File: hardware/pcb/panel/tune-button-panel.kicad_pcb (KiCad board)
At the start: 2 copper layers, 146 x 71.7 mm, 218 parts, among them J1 USB-C, J1 XIAO left, J2 LiPo, J2 XIAO right, J3 Buttons, J3 LiPo, J4 to XIAO BAT, Q1 AO3401A, SW1 MX switch, SW2 MX switch, SW3 MX switch, SW4 MX switch, SW5 RESET, SW6 BOOT, U1 ESP32-C3-WROOM-02-N4, U2 SRV05-4, U3 TP4054, U4 RT9080-3.3, U5 SRV05-4

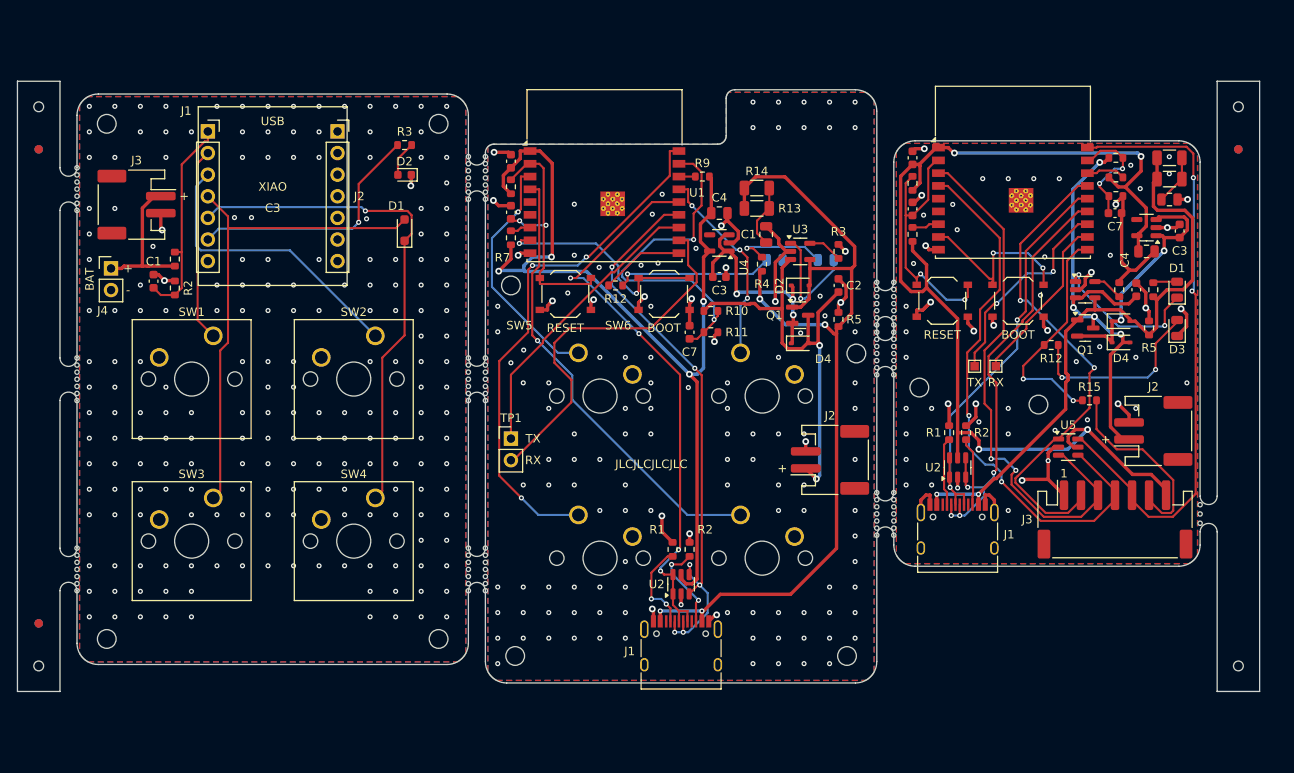
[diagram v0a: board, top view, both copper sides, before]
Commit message: pcb: panel round-1 audit fixes
A 5 mm frame (bars across the top and bottom joining the rails, clear of the overhangs),
so the right rail no longer hangs on one narrow tab. Tabs keep away from mounting holes
(a tab sat on the c3's H4) and leave room for their fillets; bites sit 0.25 mm inside the
board; tab keepouts run 1 mm past the end bites. Fiducials 3.85 mm in (JLC's minimum),
tooling holes with a 1.448 mm mask opening, only the c3's JLC marker kept, panel/fab
cleared before export. free_spans uses fab bodies (the courtyard test was never built).

route.py's crowded_pins now checks every through-hole part not reflowed in paste, not
only those without an LCSC number, so the XIAO sockets stay covered now that JLC fits
them. All three boards replay clean under it.
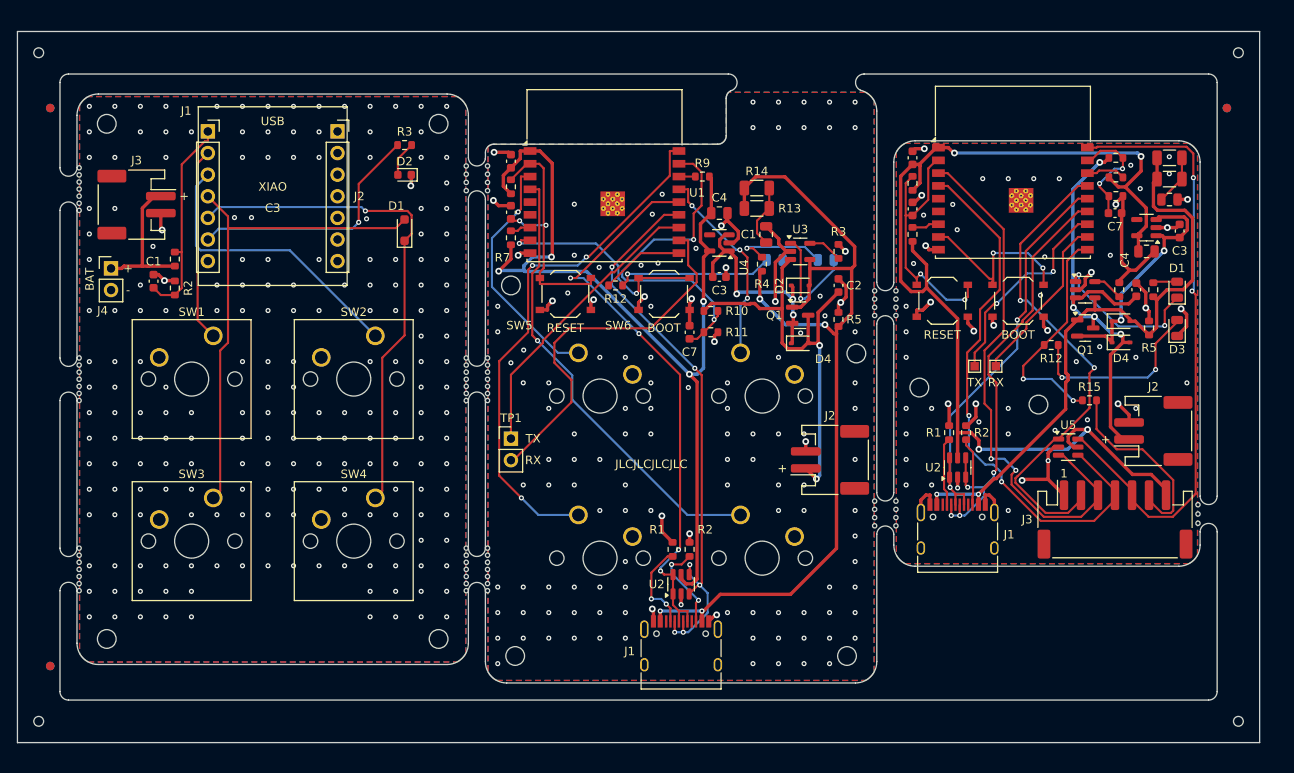
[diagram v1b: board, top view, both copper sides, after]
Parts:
- removed KiKit_MB_10_5, KiKit_MB_10_6, KiKit_MB_10_7, KiKit_MB_11_5, KiKit_MB_11_6, KiKit_MB_11_7, KiKit_MB_12_5, KiKit_MB_12_6, KiKit_MB_12_7, KiKit_MB_13_5, KiKit_MB_13_6, KiKit_MB_13_7, KiKit_MB_14_4, KiKit_MB_14_5, KiKit_MB_14_6, KiKit_MB_14_7, KiKit_MB_15_1, KiKit_MB_15_2, KiKit_MB_15_3, KiKit_MB_15_4, KiKit_MB_15_5, KiKit_MB_15_6, KiKit_MB_15_7, KiKit_MB_16_1, KiKit_MB_16_2, KiKit_MB_16_3, KiKit_MB_8_5, KiKit_MB_8_6, KiKit_MB_8_7, KiKit_MB_9_5, KiKit_MB_9_6, KiKit_MB_9_7: NPTH, NPTH
- moved KiKit_MB_9_4 47.4 mm to (55.2, 9.96)
- moved KiKit_MB_9_3 47.3 mm to (55.2, 10.9)
- moved KiKit_MB_9_2 47.2 mm to (55.2, 11.9)
- moved KiKit_MB_9_1 47.0 mm to (55.2, 12.9)
- moved KiKit_MB_7_6 46.0 mm to (55.2, 55.7)
- moved KiKit_MB_7_1 46.0 mm to (55.2, 59.9)
- moved KiKit_MB_7_2 46.0 mm to (55.2, 59.0)
- moved KiKit_MB_7_3 46.0 mm to (55.2, 58.2)
- moved KiKit_MB_7_4 46.0 mm to (55.2, 57.4)
- moved KiKit_MB_7_5 46.0 mm to (55.2, 56.5)
- moved KiKit_MB_7_7 46.0 mm to (55.2, 54.9)
- moved KiKit_MB_14_3 40.5 mm to (138.8, 52.0)
- moved KiKit_MB_14_2 39.7 mm to (138.8, 50.9)
- moved KiKit_MB_14_1 38.9 mm to (138.8, 49.8)
- moved KiKit_MB_8_1 27.7 mm to (52.8, 9.96)
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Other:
- board size 146 x 71.7 mm -> 146 x 83.6 mm

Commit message: pcb: panel round-2 audit fixes
The top bar had fused onto the c3: the milling fillets bridge any gap under two fillets.
Bars now keep 2.5 mm from every board edge as well as 1.5 mm from overhanging parts, and
panel.py checks that each board is joined only at its tabs. Every tab has fillets with
bites round them (the mill rounds them anyway), so a tab needs its width plus both fillets
of clear edge. free_spans works on all four edges, and the boards are tabbed to the top and
bottom bars where they are clear; c3-jst's right edge, which has no room once fillets count,
gets no tab, and c3-jst hangs from the c3 and the bottom bar. Tooling-hole mask expansion
0.148 mm (it was passed as the opening). crowded_pins skips SMD parts' thermal vias.
README: the panel's tabs, overhang remark.
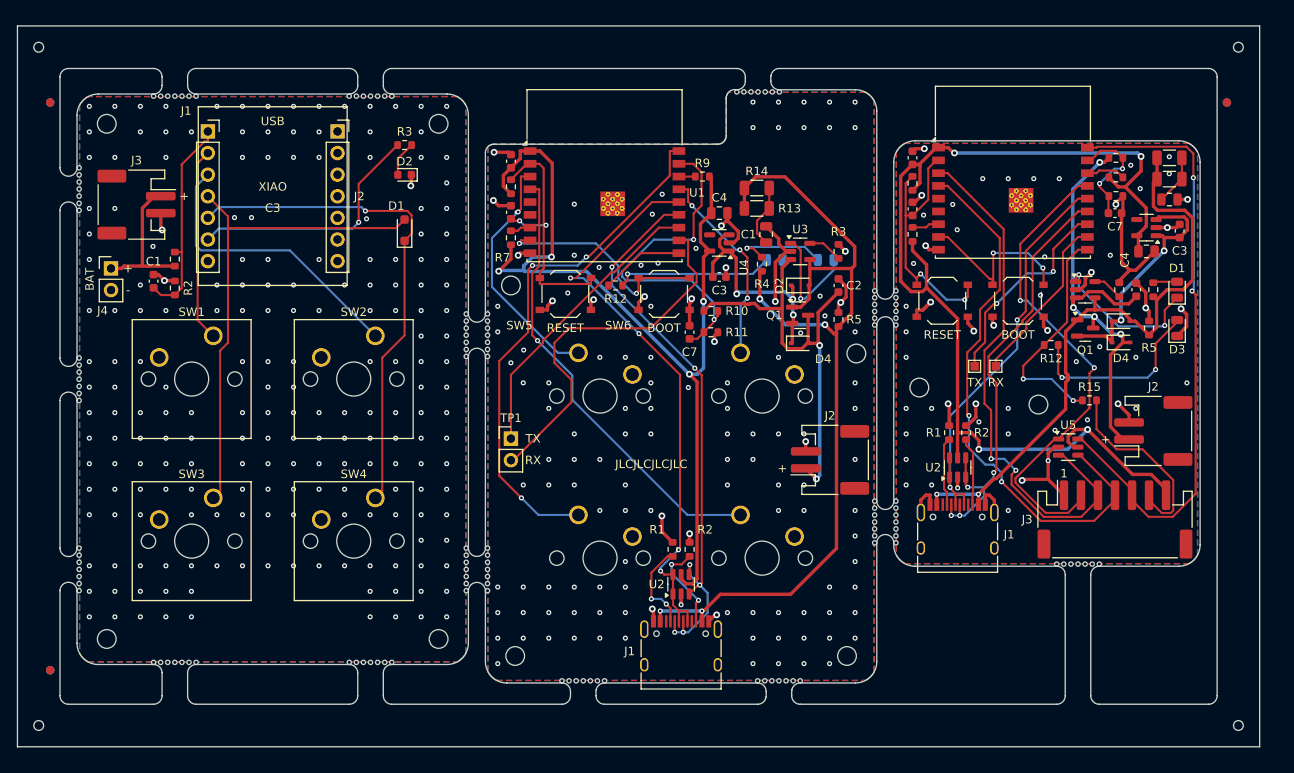
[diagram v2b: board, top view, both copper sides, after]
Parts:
- added KiKit_MB_10_5: NPTH, NPTH, F.Cu at (55.2, 29.0)
- added KiKit_MB_10_6: NPTH, NPTH, F.Cu at (55.2, 28.2)
- added KiKit_MB_10_7: NPTH, NPTH, F.Cu at (55.2, 27.3)
- added KiKit_MB_11_5: NPTH, NPTH, F.Cu at (55.2, 56.5)
- added KiKit_MB_11_6: NPTH, NPTH, F.Cu at (55.2, 55.7)
- added KiKit_MB_11_7: NPTH, NPTH, F.Cu at (55.2, 54.9)
- added KiKit_MB_12_5: NPTH, NPTH, F.Cu at (100.8, 27.8)
- added KiKit_MB_12_6: NPTH, NPTH, F.Cu at (100.8, 28.7)
- added KiKit_MB_13_5: NPTH, NPTH, F.Cu at (100.8, 52.6)
- added KiKit_MB_13_6: NPTH, NPTH, F.Cu at (100.8, 53.4)
- added KiKit_MB_13_7: NPTH, NPTH, F.Cu at (100.8, 54.3)
- added KiKit_MB_14_4: NPTH, NPTH, F.Cu at (87.0, 1.25)
- added KiKit_MB_14_5: NPTH, NPTH, F.Cu at (87.9, 1.25)
- added KiKit_MB_14_6: NPTH, NPTH, F.Cu at (88.7, 1.25)
- added KiKit_MB_14_7: NPTH, NPTH, F.Cu at (89.6, 1.25)
- added KiKit_MB_15_1: NPTH, NPTH, F.Cu at (69.0, 70.5)
- added KiKit_MB_15_2: NPTH, NPTH, F.Cu at (68.2, 70.5)
- added KiKit_MB_15_3: NPTH, NPTH, F.Cu at (67.3, 70.5)
- added KiKit_MB_15_4: NPTH, NPTH, F.Cu at (66.5, 70.5)
- added KiKit_MB_15_5: NPTH, NPTH, F.Cu at (65.7, 70.5)
- added KiKit_MB_15_6: NPTH, NPTH, F.Cu at (64.8, 70.5)
- added KiKit_MB_15_7: NPTH, NPTH, F.Cu at (64.0, 70.5)
- added KiKit_MB_16_1: NPTH, NPTH, F.Cu at (92.0, 70.5)
- added KiKit_MB_16_2: NPTH, NPTH, F.Cu at (91.2, 70.5)
- added KiKit_MB_16_3: NPTH, NPTH, F.Cu at (90.3, 70.5)
- added KiKit_MB_16_4: NPTH, NPTH, F.Cu at (89.5, 70.5)
- added KiKit_MB_16_5: NPTH, NPTH, F.Cu at (88.7, 70.5)
- added KiKit_MB_16_6: NPTH, NPTH, F.Cu at (87.8, 70.5)
- added KiKit_MB_16_7: NPTH, NPTH, F.Cu at (87.0, 70.5)
- added KiKit_MB_17_1: NPTH, NPTH, F.Cu at (103.2, 28.7)
- added KiKit_MB_17_2: NPTH, NPTH, F.Cu at (103.2, 27.8)
- added KiKit_MB_17_3: NPTH, NPTH, F.Cu at (103.2, 27.0)
- added KiKit_MB_17_4: NPTH, NPTH, F.Cu at (103.2, 26.2)
- added KiKit_MB_17_5: NPTH, NPTH, F.Cu at (103.2, 25.4)
- added KiKit_MB_17_6: NPTH, NPTH, F.Cu at (103.2, 24.6)
- added KiKit_MB_18_1: NPTH, NPTH, F.Cu at (103.2, 54.3)
- added KiKit_MB_18_2: NPTH, NPTH, F.Cu at (103.2, 53.4)
- added KiKit_MB_18_3: NPTH, NPTH, F.Cu at (103.2, 52.6)
- added KiKit_MB_18_4: NPTH, NPTH, F.Cu at (103.2, 51.8)
- added KiKit_MB_18_5: NPTH, NPTH, F.Cu at (103.2, 51.0)
- added KiKit_MB_18_6: NPTH, NPTH, F.Cu at (103.2, 50.2)
- added KiKit_MB_18_7: NPTH, NPTH, F.Cu at (103.2, 49.3)
- added KiKit_MB_19_1: NPTH, NPTH, F.Cu at (127.2, 56.8)
- added KiKit_MB_19_2: NPTH, NPTH, F.Cu at (126.3, 56.8)
- added KiKit_MB_19_3: NPTH, NPTH, F.Cu at (125.5, 56.8)
- added KiKit_MB_19_4: NPTH, NPTH, F.Cu at (124.7, 56.8)
- added KiKit_MB_19_5: NPTH, NPTH, F.Cu at (123.8, 56.8)
- added KiKit_MB_19_6: NPTH, NPTH, F.Cu at (123.0, 56.8)
- added KiKit_MB_19_7: NPTH, NPTH, F.Cu at (122.1, 56.8)
- added KiKit_MB_8_5: NPTH, NPTH, F.Cu at (17.7, 68.3)
- added KiKit_MB_8_6: NPTH, NPTH, F.Cu at (16.8, 68.3)
- added KiKit_MB_8_7: NPTH, NPTH, F.Cu at (16.0, 68.3)
- added KiKit_MB_9_5: NPTH, NPTH, F.Cu at (40.7, 68.3)
- added KiKit_MB_9_6: NPTH, NPTH, F.Cu at (39.8, 68.3)
- added KiKit_MB_9_7: NPTH, NPTH, F.Cu at (39.0, 68.3)
- moved KiKit_MB_14_3 73.0 mm to (86.2, 1.25)
- moved KiKit_MB_14_2 72.9 mm to (85.4, 1.25)
- moved KiKit_MB_14_1 72.7 mm to (84.5, 1.25)
- moved KiKit_MB_8_1 66.4 mm to (21.0, 68.3)
- moved KiKit_MB_8_2 66.0 mm to (20.2, 68.3)
- moved KiKit_MB_8_3 65.6 mm to (19.3, 68.3)
- moved KiKit_MB_8_4 65.2 mm to (18.5, 68.3)
- moved KiKit_MB_7_1 60.4 mm to (39.0, 1.75)
- moved KiKit_MB_9_4 59.9 mm to (41.5, 68.3)
- moved KiKit_MB_7_2 59.3 mm to (39.8, 1.75)
- moved KiKit_MB_9_3 58.8 mm to (42.3, 68.3)
- moved KiKit_MB_7_3 58.3 mm to (40.7, 1.75)
- moved KiKit_MB_9_2 57.7 mm to (43.2, 68.3)
- moved KiKit_MB_7_4 57.3 mm to (41.5, 1.75)
- moved KiKit_MB_9_1 56.6 mm to (44.0, 68.3)
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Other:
- board size 146 x 83.6 mm -> 146 x 84.7 mm

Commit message: pcb: panel round-3 audit fixes
Two tabs end 1.2 mm from connector anchor pads (c3 J2, c3-jst J3), inside JLC's 2 mm
keep-out, and no other edge is free there: panel.py finds tabs within 2.25 mm of a
connector's pads and puts their bites 0.25 mm outside the board, and the README says to
cut those two with flush cutters. 6 mm rails and bars, so the fiducials sit 4.35 mm in
(JLC's 3.35 mm to the opening). The self-check now tests each piece of material along a
board's edge against its own tab, not a per-board total. Bite pitch 0.75 mm. README:
mounting-hole wording matches the 2 mm rule.
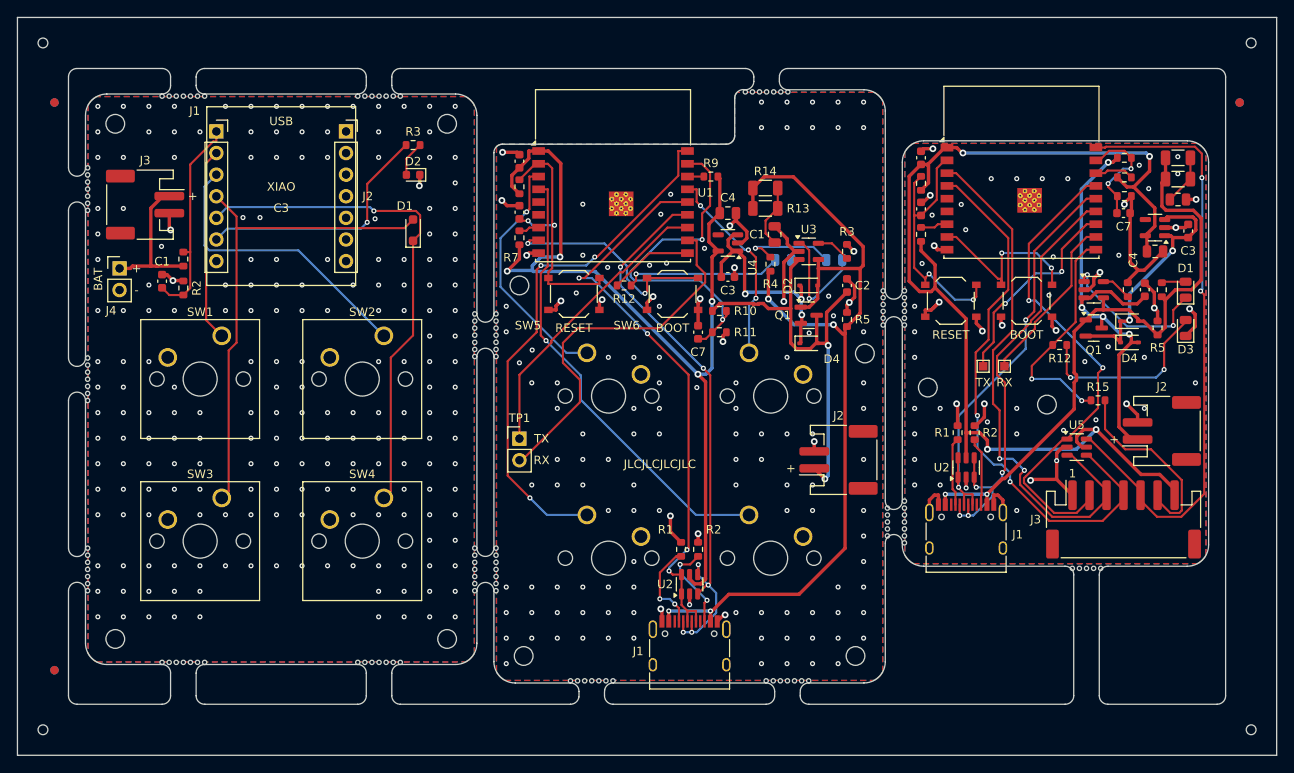
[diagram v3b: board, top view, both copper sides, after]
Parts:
- removed the C1 at (135.4, 13.9)
- removed the C1 at (88.0, 18.0)
- removed the C1 at (16.0, 23.5)
- removed the C2 at (131.5, 24.5)
- removed the C2 at (96.5, 24.0)
- removed the C3 at (82.5, 23.0)
- removed the C3 at (136.6, 17.6)
- removed the C4 at (82.5, 15.5)
- removed the C4 at (132.7, 20.0)
- removed the C5 at (105.2, 9.00)
- removed the C5 at (58.0, 9.40)
- removed the C6 at (58.0, 15.4)
- removed the C6 at (105.2, 15.0)
- removed the C7 at (129.0, 15.5)
- removed the C7 at (79.0, 29.5)
- removed the D1 at (136.3, 24.5)
- removed the D1 at (45.5, 17.5)
- removed the D1 at (95.0, 21.0)
- removed the D2 at (92.0, 24.0)
- removed the D2 at (129.7, 28.2)
- removed the D2 at (45.5, 11.0)
- removed the D3 at (136.3, 29.0)
- removed the D3 at (89.0, 21.0)
- removed the D4 at (92.0, 30.8)
- removed the D4 at (129.7, 30.7)
- removed the H1 at (97.5, 67.5)
- removed the H1 at (10.5, 5.00)
- removed the H1 at (106.0, 36.0)
- removed the H2 at (49.5, 5.00)
- removed the H2 at (58.5, 67.5)
- removed the H2 at (120.0, 38.0)
- removed the H3 at (10.5, 65.5)
- removed the H3 at (58.0, 24.0)
- removed the H4 at (49.5, 65.5)
- removed the H4 at (98.6, 32.0)
- removed the J1 at (22.4, 5.90)
- removed the J1 at (78.0, 67.5)
- removed the J1 at (110.5, 53.8)
- removed the J2 at (95.5, 44.5)
- removed the J2 at (37.6, 5.90)
- removed the J2 at (133.5, 41.1)
- removed the J3 at (14.0, 14.5)
- removed the J3 at (129.0, 51.5)
- removed KiKit_MB_16_7, KiKit_MB_18_1, KiKit_MB_18_7, KiKit_MB_19_1, KiKit_MB_19_7: NPTH, NPTH
- removed the Q1 at (125.5, 29.0)
- removed the Q1 at (92.0, 27.5)
- removed the R1 at (18.5, 20.9)
- removed the R1 at (109.5, 41.3)
- removed the R1 at (77.0, 55.0)
- removed the R10 at (81.5, 27.0)
- removed the R10 at (129.1, 9.00)
- removed the R11 at (129.1, 13.5)
- removed the R11 at (81.5, 29.5)
- removed the R12 at (121.5, 31.0)
- removed the R12 at (70.3, 24.0)
- removed the R13 at (135.4, 9.00)
- removed the R13 at (86.9, 14.9)
- removed the R14 at (86.9, 12.6)
- removed the R14 at (135.4, 11.5)
- removed the R2 at (18.5, 24.3)
- removed the R2 at (79.0, 55.0)
- removed the R2 at (111.5, 41.3)
- removed the R3 at (129.5, 24.5)
- removed the R3 at (96.5, 20.0)
- removed the R3 at (45.5, 7.50)
- removed the R4 at (87.5, 21.5)
- removed the R4 at (133.5, 24.5)
- removed the R5 at (133.0, 29.0)
- removed the R5 at (96.5, 28.0)
- removed the R6 at (105.2, 12.0)
- removed the R6 at (58.0, 12.4)
- removed the R7 at (105.2, 18.0)
- removed the R7 at (58.0, 18.4)
- removed the R9 at (80.5, 11.2)
- removed the R9 at (129.1, 11.3)
- removed the SW1 at (23.0, 29.9)
- removed the SW1 at (85.0, 31.9)
- removed the SW2 at (42.1, 29.9)
- removed the SW2 at (65.9, 31.9)
- removed the SW3 at (23.0, 49.0)
- removed the SW3 at (85.0, 51.0)
- removed the SW4 at (42.1, 49.0)
- removed the SW4 at (65.9, 51.0)
- removed the SW5 at (108.7, 25.8)
- removed the SW5 at (64.4, 25.0)
- removed the SW6 at (117.6, 25.8)
- removed the SW6 at (76.0, 25.0)
- removed the TP1 at (112.5, 33.5)
- removed the TP1 at (58.0, 42.0)
- removed the U1 at (69.0, 14.2)
- removed the U1 at (117.0, 13.8)
- removed the U2 at (110.5, 45.4)
- removed the U2 at (78.0, 59.1)
- removed the U3 at (92.0, 20.0)
- removed the U3 at (125.5, 24.5)
- removed the U4 at (132.7, 17.2)
- removed the U4 at (82.5, 19.0)
- added C1: 10u, Capacitor_SMD:C_0805_2012Metric, F.Cu at (136.4, 13.9)
- added C1: 100n, Capacitor_SMD:C_0603_1608Metric, F.Cu at (17.0, 23.5)
- added C1: 10u, Capacitor_SMD:C_0805_2012Metric, F.Cu at (89.0, 18.0)
- added C2: 4.7u, Capacitor_SMD:C_0603_1608Metric, F.Cu at (97.5, 24.0)
- added C2: 4.7u, Capacitor_SMD:C_0603_1608Metric, F.Cu at (132.5, 24.5)
- added C3: 1u, Capacitor_SMD:C_0603_1608Metric, F.Cu at (137.6, 17.6)
- added C3: 1u, Capacitor_SMD:C_0603_1608Metric, F.Cu at (83.5, 23.0)
- added C4: 22u, Capacitor_SMD:C_0805_2012Metric, F.Cu at (83.5, 15.5)
- added C4: 22u, Capacitor_SMD:C_0805_2012Metric, F.Cu at (133.7, 20.0)
- added C5: 100n, Capacitor_SMD:C_0603_1608Metric, F.Cu at (106.2, 9.00)
- added C5: 100n, Capacitor_SMD:C_0603_1608Metric, F.Cu at (59.0, 9.40)
- added C6: 1u, Capacitor_SMD:C_0603_1608Metric, F.Cu at (106.2, 15.0)
- added C6: 1u, Capacitor_SMD:C_0603_1608Metric, F.Cu at (59.0, 15.4)
- added C7: 100n, Capacitor_SMD:C_0603_1608Metric, F.Cu at (80.0, 29.5)
- added C7: 100n, Capacitor_SMD:C_0603_1608Metric, F.Cu at (130.0, 15.5)
- added D1: 1N4148WS, Diode_SMD:D_SOD-323_HandSoldering, F.Cu at (46.5, 17.5)
- added D1: CHG red, LED_SMD:LED_0805_2012Metric, F.Cu at (137.3, 24.5)
- added D1: CHG red, LED_SMD:LED_0805_2012Metric, B.Cu at (96.0, 21.0)
- added D2: 1N5819WS, Diode_SMD:D_SOD-323, F.Cu at (93.0, 24.0)
- added D2: 1N5819WS, Diode_SMD:D_SOD-323, F.Cu at (130.7, 28.2)
- added D2: LED, LED_SMD:LED_0603_1608Metric, F.Cu at (46.5, 11.0)
- added D3: LED, LED_SMD:LED_0805_2012Metric, F.Cu at (137.3, 29.0)
- added D3: LED, LED_SMD:LED_0805_2012Metric, B.Cu at (90.0, 21.0)
- added D4: 1N5819WS, Diode_SMD:D_SOD-323, F.Cu at (130.7, 30.7)
- added D4: 1N5819WS, Diode_SMD:D_SOD-323, F.Cu at (93.0, 30.8)
- added H1: M2, MountingHole:MountingHole_2.2mm_M2, F.Cu at (107.0, 36.0)
- added H1: M2, MountingHole:MountingHole_2.2mm_M2, F.Cu at (11.5, 5.00)
- added H1: M2, MountingHole:MountingHole_2.2mm_M2, F.Cu at (98.5, 67.5)
- added H2: M2, MountingHole:MountingHole_2.2mm_M2, F.Cu at (59.5, 67.5)
- added H2: M2, MountingHole:MountingHole_2.2mm_M2, F.Cu at (50.5, 5.00)
- added H2: M2, MountingHole:MountingHole_2.2mm_M2, F.Cu at (121.0, 38.0)
- added H3: M2, MountingHole:MountingHole_2.2mm_M2, F.Cu at (11.5, 65.5)
- added H3: M2, MountingHole:MountingHole_2.2mm_M2, F.Cu at (59.0, 24.0)
- added H4: M2, MountingHole:MountingHole_2.2mm_M2, F.Cu at (50.5, 65.5)
- added H4: M2, MountingHole:MountingHole_2.2mm_M2, F.Cu at (99.6, 32.0)
- added J1: XIAO left, Connector_PinSocket_2.54mm:PinSocket_1x07_P2.54mm_Vertical, F.Cu at (23.4, 5.90)
- added J1: USB-C, Connector_USB:USB_C_Receptacle_HRO_TYPE-C-31-M-12, F.Cu at (79.0, 67.5)
- added J1: USB-C, Connector_USB:USB_C_Receptacle_HRO_TYPE-C-31-M-12, F.Cu at (111.5, 53.8)
- added J2: LiPo, Connector_JST:JST_PH_S2B-PH-SM4-TB_1x02-1MP_P2.00mm_Horizontal, F.Cu at (134.5, 41.1)
- added J2: LiPo, Connector_JST:JST_PH_S2B-PH-SM4-TB_1x02-1MP_P2.00mm_Horizontal, F.Cu at (96.5, 44.5)
- added J2: XIAO right, Connector_PinSocket_2.54mm:PinSocket_1x07_P2.54mm_Vertical, F.Cu at (38.6, 5.90)
- added J3: Buttons, Connector_JST:JST_PH_S7B-PH-SM4-TB_1x07-1MP_P2.00mm_Horizontal, F.Cu at (130.0, 51.5)
- added J3: LiPo, Connector_JST:JST_PH_S2B-PH-SM4-TB_1x02-1MP_P2.00mm_Horizontal, F.Cu at (15.0, 14.5)
- added KiKit_MB_17_7: NPTH, NPTH, F.Cu at (104.2, 49.3)
- added Q1: AO3401A, Package_TO_SOT_SMD:SOT-23, F.Cu at (93.0, 27.5)
- added Q1: AO3401A, Package_TO_SOT_SMD:SOT-23, F.Cu at (126.5, 29.0)
- added R1: 5.1k, Resistor_SMD:R_0603_1608Metric, F.Cu at (110.5, 41.3)
- added R1: 220k, Resistor_SMD:R_0603_1608Metric, F.Cu at (19.5, 20.9)
- added R1: 5.1k, Resistor_SMD:R_0603_1608Metric, F.Cu at (78.0, 55.0)
- added R10: 220k, Resistor_SMD:R_0603_1608Metric, F.Cu at (130.1, 9.00)
- added R10: 220k, Resistor_SMD:R_0603_1608Metric, F.Cu at (82.5, 27.0)
- added R11: 220k, Resistor_SMD:R_0603_1608Metric, F.Cu at (130.1, 13.5)
- added R11: 220k, Resistor_SMD:R_0603_1608Metric, F.Cu at (82.5, 29.5)
- added R12: 1k, Resistor_SMD:R_0603_1608Metric, F.Cu at (71.3, 24.0)
- added R12: 1k, Resistor_SMD:R_0603_1608Metric, F.Cu at (122.5, 31.0)
- added R13: 1, Resistor_SMD:R_1206_3216Metric, F.Cu at (87.9, 14.9)
- added R13: 1, Resistor_SMD:R_1206_3216Metric, F.Cu at (136.4, 9.00)
- added R14: 1, Resistor_SMD:R_1206_3216Metric, F.Cu at (136.4, 11.5)
- added R14: 1, Resistor_SMD:R_1206_3216Metric, F.Cu at (87.9, 12.6)
- added R2: 5.1k, Resistor_SMD:R_0603_1608Metric, F.Cu at (80.0, 55.0)
- added R2: 5.1k, Resistor_SMD:R_0603_1608Metric, F.Cu at (112.5, 41.3)
- added R2: 220k, Resistor_SMD:R_0603_1608Metric, F.Cu at (19.5, 24.3)
- added R3: 4.7k, Resistor_SMD:R_0603_1608Metric, F.Cu at (130.5, 24.5)
- added R3: 1k, Resistor_SMD:R_0603_1608Metric, F.Cu at (46.5, 7.50)
- added R3: 4.7k, Resistor_SMD:R_0603_1608Metric, F.Cu at (97.5, 20.0)
- added R4: 1k, Resistor_SMD:R_0603_1608Metric, F.Cu at (88.5, 21.5)
- added R4: 1k, Resistor_SMD:R_0603_1608Metric, F.Cu at (134.5, 24.5)
- added R5: 3.3k, Resistor_SMD:R_0603_1608Metric, F.Cu at (134.0, 29.0)
- added R5: 3.3k, Resistor_SMD:R_0603_1608Metric, F.Cu at (97.5, 28.0)
- added R6: 10k, Resistor_SMD:R_0603_1608Metric, F.Cu at (106.2, 12.0)
- added R6: 10k, Resistor_SMD:R_0603_1608Metric, F.Cu at (59.0, 12.4)
- added R7: 10k, Resistor_SMD:R_0603_1608Metric, F.Cu at (106.2, 18.0)
- added R7: 10k, Resistor_SMD:R_0603_1608Metric, F.Cu at (59.0, 18.4)
- added R9: 10k, Resistor_SMD:R_0603_1608Metric, F.Cu at (130.1, 11.3)
- added R9: 10k, Resistor_SMD:R_0603_1608Metric, F.Cu at (81.5, 11.2)
- added SW1: MX switch, Button_Switch_Keyboard:SW_Cherry_MX_1.00u_PCB, F.Cu at (24.0, 29.9)
- added SW1: MX switch, Button_Switch_Keyboard:SW_Cherry_MX_1.00u_PCB, B.Cu at (86.0, 31.9)
- added SW2: MX switch, Button_Switch_Keyboard:SW_Cherry_MX_1.00u_PCB, F.Cu at (43.1, 29.9)
- added SW2: MX switch, Button_Switch_Keyboard:SW_Cherry_MX_1.00u_PCB, B.Cu at (66.9, 31.9)
- added SW3: MX switch, Button_Switch_Keyboard:SW_Cherry_MX_1.00u_PCB, F.Cu at (24.0, 49.0)
- added SW3: MX switch, Button_Switch_Keyboard:SW_Cherry_MX_1.00u_PCB, B.Cu at (86.0, 51.0)
- added SW4: MX switch, Button_Switch_Keyboard:SW_Cherry_MX_1.00u_PCB, F.Cu at (43.1, 49.0)
- added SW4: MX switch, Button_Switch_Keyboard:SW_Cherry_MX_1.00u_PCB, B.Cu at (66.9, 51.0)
- added SW5: RESET, Button_Switch_SMD:SW_Push_1P1T_XKB_TS-1187A, F.Cu at (109.7, 25.8)
- added SW5: RESET, Button_Switch_SMD:SW_Push_1P1T_XKB_TS-1187A, F.Cu at (65.4, 25.0)
- added SW6: BOOT, Button_Switch_SMD:SW_Push_1P1T_XKB_TS-1187A, F.Cu at (118.6, 25.8)
- added SW6: BOOT, Button_Switch_SMD:SW_Push_1P1T_XKB_TS-1187A, F.Cu at (77.0, 25.0)
- added TP1: UART, Connector_PinHeader_2.54mm:PinHeader_1x02_P2.54mm_Vertical, F.Cu at (59.0, 42.0)
- added TP1: TXD, TestPoint:TestPoint_Pad_1.0x1.0mm, F.Cu at (113.5, 33.5)
- added U1: ESP32-C3-WROOM-02-N4, RF_Module:ESP32-C3-WROOM-02, F.Cu at (118.0, 13.8)
- added U1: ESP32-C3-WROOM-02-N4, RF_Module:ESP32-C3-WROOM-02, F.Cu at (70.0, 14.2)
- added U2: SRV05-4, Package_TO_SOT_SMD:SOT-23-6, F.Cu at (79.0, 59.1)
- added U2: SRV05-4, Package_TO_SOT_SMD:SOT-23-6, F.Cu at (111.5, 45.4)
- added U3: TP4054, Package_TO_SOT_SMD:SOT-23-5, F.Cu at (93.0, 20.0)
- added U3: TP4054, Package_TO_SOT_SMD:SOT-23-5, F.Cu at (126.5, 24.5)
- added U4: RT9080-3.3, Package_TO_SOT_SMD:SOT-23-5, F.Cu at (133.7, 17.2)
- added U4: RT9080-3.3, Package_TO_SOT_SMD:SOT-23-5, F.Cu at (83.5, 19.0)
- moved KiKit_MB_14_7 73.4 mm to (65.0, 70.5)
- moved KiKit_MB_14_6 72.9 mm to (65.8, 70.5)
- moved KiKit_MB_14_5 72.4 mm to (66.7, 70.5)
- moved KiKit_MB_14_4 71.9 mm to (67.5, 70.5)
- moved KiKit_MB_14_3 71.5 mm to (68.3, 70.5)
- moved KiKit_MB_14_2 71.1 mm to (69.2, 70.5)
- moved KiKit_MB_14_1 70.7 mm to (70.0, 70.5)
- moved KiKit_MB_13_7 54.0 mm to (90.6, 1.25)
- moved KiKit_MB_13_6 53.3 mm to (89.7, 1.25)
- moved KiKit_MB_13_5 52.7 mm to (88.9, 1.25)
- moved KiKit_MB_13_4 52.1 mm to (88.0, 1.25)
- moved KiKit_MB_13_3 51.5 mm to (87.2, 1.25)
- moved KiKit_MB_13_2 51.0 mm to (86.4, 1.25)
- moved KiKit_MB_13_1 50.4 mm to (85.5, 1.25)
- moved KiKit_MB_16_6 48.7 mm to (104.2, 24.6)
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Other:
- board size 146 x 84.7 mm -> 148 x 86.7 mm
